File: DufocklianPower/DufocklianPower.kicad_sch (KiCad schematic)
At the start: 84 parts, among them J1 Conn_Receptacle_3P_Protected, J2 ST7796S, Q1 NMOS, Q2 NMOS, SW1 RST, SW2 BOOT, T1 Transformer_1P_1S, U2 LM5164DDA, U3 OPA388, U4 AD5282, U5 MCP4725, U6 ESP32-S3-WROOM-1, U7 INA228

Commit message: plotted again
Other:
- note added: "BUCK BOOST CONTROLLER"
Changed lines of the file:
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@@
+		)
+	)
+	(text "BUCK BOOST CONTROLLER"
+		(exclude_from_sim no)
+		(at 173.228 73.66 0)
+		(effects
+			(font
+				(size 1.27 1.27)
+			)
 		)
 	)

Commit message: finish pcb
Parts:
- removed C12: 1n, symbol Device:C
- removed C13, C29, C33, C34: 100n, symbol Device:C
- removed C14: 100u, symbol Device:C
- removed C28: 22n, symbol Device:C
- removed C30, C31, C32: 220u, symbol Device:C
- removed C35: 10u, symbol Device:C
- removed C4, C5: 10m, symbol Device:C
- removed D1: ABS2, Diode_SMD:Diode_Bridge_Diotec_ABS, symbol Diode_Bridge:ABS2
- removed D2: BAT54W, Package_TO_SOT_SMD:SOT-323_SC-70, symbol Diode:BAT54W
- removed J1: Conn_Receptacle_3P_Protected, symbol Connector:Conn_Receptacle_3P_Protected
- removed J2: ST7796S, symbol Connector_Generic:Conn_01x09
- removed L3: 1.5uH, symbol Device:L
- removed R15, R18: 11k, symbol Device:R
- removed R23: 6040, symbol Device:R
- removed T1: Transformer_1P_1S, symbol Device:Transformer_1P_1S
- removed U3: OPA388, Package_SO:SOIC-8_3.9x4.9mm_P1.27mm, symbol Amplifier_Operational:OPA333xxD
- removed U4: AD5282, Package_SO:TSSOP-16_4.4x5mm_P0.65mm, symbol Potentiometer_Digital:AD5282
- removed U5: MCP4725, Package_TO_SOT_SMD:SOT-23-6, symbol Analog_DAC:MCP4725xxx-xCH
- removed U7: INA228, Package_SO:TSSOP-10_3x3mm_P0.5mm, symbol Sensor_Energy:INA228
- added C4: 1u, Capacitor_SMD:C_0805_2012Metric, symbol Device:C_Small
- added C40: 100n, Capacitor_SMD:C_0805_2012Metric, symbol Device:C
- added C42: 100p, Capacitor_SMD:C_0805_2012Metric, symbol Device:C
- added C43: 1n, Capacitor_SMD:C_0805_2012Metric, symbol Device:C
- added C44: 2.2n, Capacitor_SMD:C_0805_2012Metric, symbol Device:C
- added J1, J3: 8174, Library:KEYSTONE_8174, symbol dufocklpwr:8174
- added J2: SCREEN, Connector_PinHeader_2.54mm:PinHeader_1x04_P2.54mm_Vertical, symbol Connector:Conn_01x04_Pin
- added J4: USB_C_Receptacle_USB2.0_14P, Connector_USB:USB_C_Receptacle_GCT_USB4105-xx-A_16P_TopMnt_Horizontal, symbol Connector:USB_C_Receptacle_USB2.0_14P
- added J5: OUT, Connector_AMASS:AMASS_XT60PW-M_1x02_P7.20mm_Horizontal, symbol Connector:Screw_Terminal_01x02
- added Q4: 2N7002, Package_TO_SOT_SMD:SOT-23, symbol Transistor_FET:2N7002
- added R23, R28: 2m, Library:FC4L90_OHM, symbol Device:R_Shunt
- added R29, R35: 2.7k, Resistor_SMD:R_0603_1608Metric, symbol Device:R
- added R30, R31: 5.1k, Resistor_SMD:R_0603_1608Metric, symbol Device:R
- added R32: 100k, Resistor_SMD:R_0603_1608Metric, symbol Device:R_45deg
- added R33, R34: 100, Resistor_SMD:R_0603_1608Metric, symbol Device:R_Small
- added SW3: Voltage Control, Rotary_Encoder:RotaryEncoder_Alps_EC11E-Switch_Vertical_H20mm, symbol Device:RotaryEncoder_Switch
- added SW4: Current Control, Rotary_Encoder:RotaryEncoder_Alps_EC11E-Switch_Vertical_H20mm, symbol Device:RotaryEncoder_Switch
- added U11: INA228, Package_SO:TSSOP-10_3x3mm_P0.5mm, symbol Sensor_Energy:INA228
- added U3: ADS8681RUM, Package_DFN_QFN:QFN-16-1EP_4x4mm_P0.65mm_EP2.7x2.7mm, symbol Analog_ADC:ADS8681RUM
- added U4: DAC8562, Package_SO:TSSOP-10_3x3mm_P0.5mm, symbol dufocklpwr:DAC8562
- added U5: INA241A4xD, Package_SO:SOIC-8_3.9x4.9mm_P1.27mm, symbol Amplifier_Current:INA241A4xD
- added U7: OPA188xxD, Package_SO:SOIC-8_3.9x4.9mm_P1.27mm, symbol Amplifier_Operational:OPA188xxD
- added U8: AP2112K-3.3, Package_TO_SOT_SMD:SOT-23-5, symbol Regulator_Linear:AP2112K-3.3
- added U9: REF6025xDGK, Package_SO:VSSOP-8_3x3mm_P0.65mm, symbol Reference_Voltage:REF6025xDGK
- C1, C19, C25, C36, C37, C38, C6, C7, C8: footprint (none) -> Capacitor_SMD:C_0805_2012Metric
- C10: value 470n -> 4.7u; footprint (none) -> Capacitor_SMD:C_0805_2012Metric
- C11: value 10n -> 10u; footprint (none) -> Capacitor_SMD:C_0805_2012Metric
- C15, C16, C17, C18, C21, C22, C23, C24: footprint (none) -> Capacitor_SMD:C_1210_3225Metric
- C2, C3: value 10m -> 1u; footprint (none) -> Capacitor_SMD:C_0805_2012Metric
- C20, C9: value 100n -> 1u; footprint (none) -> Capacitor_SMD:C_0805_2012Metric
- C26: value 2.2n -> 1u; footprint (none) -> Capacitor_SMD:C_0805_2012Metric
- C27: value 2.2n -> 47u; footprint (none) -> Capacitor_SMD:C_0805_2012Metric
- L1: footprint (none) -> Library:IND_SER2915H-223KL
- L2: footprint (none) -> Library:IND_BOURNS_SRR1260
- Q1, Q2: footprint (none) -> Library:TRANS_BSC027N10NS5ATMA1
- R1, R12, R13, R16, R17, R2, R24, R25, R26, R27, R3, R6: footprint (none) -> Resistor_SMD:R_0603_1608Metric
- R10: value 50k -> 14k7; footprint (none) -> Resistor_SMD:R_0603_1608Metric
- R11: value 470m -> 400k; footprint (none) -> Resistor_SMD:R_0603_1608Metric
- R14: value 1k -> 100k; footprint (none) -> Resistor_SMD:R_0603_1608Metric
- R19: value 10m -> 10k; footprint (none) -> Resistor_SMD:R_0603_1608Metric
- R20: value 121k -> 4.7k; footprint (none) -> Resistor_SMD:R_0603_1608Metric
- R21: value 1960 -> 120k; footprint (none) -> Resistor_SMD:R_0603_1608Metric
- R22: value 50 -> 5m; footprint (none) -> Resistor_SMD:R_0603_1608Metric
- R4: value 350k -> 316k; footprint (none) -> Resistor_SMD:R_0603_1608Metric
- R5: value 200k -> 101k; footprint (none) -> Resistor_SMD:R_0603_1608Metric
- R7: footprint (none) -> Resistor_SMD:R_2512_6332Metric
- R8: value 15 -> 615k; footprint (none) -> Resistor_SMD:R_0603_1608Metric
- R9: value 1k -> 10k; footprint (none) -> Resistor_SMD:R_0603_1608Metric
- SW1, SW2: footprint (none) -> Button_Switch_SMD:SW_Push_1P1T-SH_NO_CK_KMR2xxG
- U1: footprint (none) -> Library:VQFN24_RGY_TEX
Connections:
- net +3V3: now also C3.1, R26.1, C40.1, J2.2 (Pin_2), R29.1, R35.1, U11.6 (VS), U3.14 (DVDD), U4.9 (VDD), U8.5 (VOUT); no longer C6.2, L2.2, R26.2, R4.1
- net D+: now also J4.A6 (D+), J4.B6 (D+)
- net D-: now also J4.A7 (D-), J4.B7 (D-)
- net FB: now also R10.2, R8.2, R9.1; no longer R14.1
- net GND: now also C1.2, C10.1, C11.1, C15.2, C16.2, C17.2, C18.2, C19.2, C2.2, C20.2, C21.2, C22.2, C23.2, C24.2, C26.2, C27.2, C3.2, C36.2, C37.2, C38.2, C9.1, Q2.3 (S), R1.2, R13.2, R14.2, R21.2, R3.2, R5.2, R9.2, SW1.1, SW2.1, U1.1 (AVSS), U1.10 (PGND), U1.16 (VCCX), U1.18 (PFM/SYNC), U1.24 (REFAGND), U1.25 (GND), U1.7 (AGND), U2.1 (GND), U2.9 (EP), U6.1 (GND), U6.40 (GND), U6.41 (GND), C40.2, C44.1, J2.1 (Pin_1), J3.1, J3.2 (1__1), J3.3 (1__2), J3.4 (1__3), J4.A1 (GND), J4.A12 (GND), J4.B1 (GND), J4.B12 (GND), J4.SH (SHIELD), J5.1 (Pin_1), Q4.2 (S), R30.1, R31.2, R32.2, SW3.C, SW3.S2, SW4.C, SW4.S2, U11.1 (A1), U11.2 (A0), U11.7 (GND), U3.1 (AGND), U3.15 (DGND), U3.17 (PAD), U3.3 (REFGND), U3.6 (AIN_GND), U4.3 (GND), U5.2 (GND), U5.3 (REF2), U5.4 (GND), U5.7 (REF1), U7.4 (V-), U8.2 (GND), U9.7 (GND_F), U9.8 (GND_S); no longer R19.2
- net SCL: now also U6.11 (IO18), J2.3 (Pin_3), U11.5 (SCL); no longer U6.17 (IO9)
- net SDA: now also R26.2, U6.10 (IO17), J2.4 (Pin_4), U11.4 (SDA); no longer R26.1, U6.12 (IO8)
- net VBUS: now also C15.1, C16.1, C17.1, C18.1, Q1.1 (D), U1.12 (VIN), J1.1, J1.2 (1__1), J1.3 (1__2), J1.4 (1__3); no longer C10.1, C2.1, C3.1, C9.1, R11.1
- net VOUT_{0}: now also R11.2, R8.1, R23.1, R23.2, U5.8 (+); no longer R22.1
- net ~{ALRT}: now also U6.12 (IO8), U11.3 (~{Alert}); no longer U6.35 (IO42)
- net at R22.2: now also C27.1; no longer R20.1
- net at R20.2: now also Q4.3 (D); no longer R21.1
- net COMP: now reaches C36.1, R2.1, U1.5 (EXTCOMP)
- net COMP: now also R20.1
- net D_{IN}: now reaches U6.15 (IO3)
- net D_{IN}: now also U4.8 (D_{IN})
- net SCLK: now reaches U6.16 (IO46)
- net SCLK: now also U4.7 (SCLK)
- net ~{LDAC}: now reaches U6.18 (IO10)
- net ~{LDAC}: now also U4.4 (~{LDAC})
- net ~{CLR}: now reaches U6.19 (IO11)
- net ~{CLR}: now also U4.5 (~{CLR})
- net CEN_{A}: now reaches U6.23 (IO21)
- net CEN_{A}: now also SW4.A
- net VEN_{A}: now reaches U6.24 (IO47)
- net VEN_{A}: now also SW3.A
- net VEN_{B}: now reaches U6.25 (IO48)
- net VEN_{B}: now also SW3.B
- net V_{CF}: now reaches U6.26 (IO45)
- net V_{CF}: now also R29.2, SW3.S1
- net RVS: now reaches U6.31 (IO38)
- net RVS: now also U3.13 (RVS)
- net ALR: now reaches U6.32 (IO39)
- net ALR: now also U3.12 (SDO-1)
- net SDI: now reaches U6.38 (IO2)
- net SDI: now also U3.8 (SDI)
- net ~{RST}: now reaches U6.39 (IO1)
- net ~{RST}: now also U3.7 (~{RST})
- net BL renamed C_{CF}
- net C_{CF}: now also R35.2, SW4.S1
- net CS renamed CEN_{B}
- net CEN_{B}: now also SW4.B
- net DC: no longer names the net of U6.8 (IO15)
- removed net GNDREF: C1.2, C15.2, C16.2, C17.2, C18.2, C19.2, C2.2, C20.2, C21.2, C22.2, C23.2, C24.2, C3.2, C36.2, C37.2, C38.2, Q2.3 (S), R1.2, R13.2, R19.1, R21.2, R24.1, R3.2, R5.2, SW1.1, SW2.1, U1.1 (AVSS), U1.10 (PGND), U1.16 (VCCX), U1.18 (PFM/SYNC), U1.24 (REFAGND), U1.7 (AGND), U2.1 (GND), U2.9 (EP), U6.1 (GND), U6.40 (GND), U6.41 (GND)
- removed net INJ: C11.2, R10.2, R8.1, R9.1, U1.2 (INJ)
- removed net R1_{IN}: C26.2, C27.1, R16.2
- net R2_{IN}: no longer names the net of R24.2
- net R2_{IN}: now also Q4.1 (G), R32.1; no longer C27.2
- net RST: no longer names the net of U6.9 (IO16)
- net SDA_{0} renamed EN
- net EN: now also U1.19 (EN)
- removed net SENSE: C9.2, R10.1, U1.23 (SENSE)
- removed net VCC: C15.1, C16.1, C17.1, C18.1, Q1.1 (D), U1.12 (VIN), U1.19 (EN)
- net W_{1} renamed SDO
- net SDO: now also U3.11 (SDO-0)
- net W_{2} renamed CLK
- net CLK: now also U3.10 (SCLK)
- new net: C4.1, R34.1, U11.10 (Vin+)
- new net: C10.2, U3.2 (REFIO)
- new net: C4.2, R33.1, U11.9 (Vin-)
- new net: C42.1, C44.2, R16.2, R19.1, U7.3 (+)
- new net: C42.2, C43.2, R24.1, U7.6
- new net: J4.B5 (CC2), R30.2
- new net: R11.1, R14.1, U3.5 (AIN_P)
- new net: C43.1, R19.2
- new net: C11.2, C9.2, U3.4 (REFCAP)
- new net: C26.1, U9.4 (FILT)
- new net: J4.A5 (CC1), R31.1
- new net: R16.1, U5.5
- new net: R21.1, U9.3 (SS)
- new net +5V: C2.1, C6.2, J4.A4 (VBUS), J4.A9 (VBUS), J4.B4 (VBUS), J4.B9 (VBUS), L2.2, R4.1, U3.16 (AVDD), U5.6 (V+), U7.7 (V+), U8.1 (VIN), U8.3 (EN), U9.1 (VIN), U9.2 (EN)
- new net VOUT: J5.2 (Pin_2), R28.3, R28.4, R33.2
- new net VOUT_{1}: R23.3, R23.4, R28.1, R28.2, R34.2, U11.8 (Vbus), U5.1 (-)
- new net V_{REF}: R22.1, U4.10 (V_{REF}), U9.5 (OUT_S), U9.6 (OUT_F)
- new net ~{CC_{REF}}: U4.2 (V_{OUT}B), U7.2 (-)
- new net ~{CS}: U3.9 (CONVST/~{CS}), U6.35 (IO42)
- new net ~{SYNC}: U4.6 (~{SYNC}), U6.17 (IO9)
- new net ~{VC_{REF}}: R10.1, U4.1 (V_{OUT}A)
- no-connect marks 25 -> 14
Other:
- note added: "CC LOOP + COMP CLAMP"
- note added: "DIVIDER"
- note added: "Interface"
- note added: "POWER MOUNTS"
- note added: "REF DAC"
- note added: "REFERENCE VOLTAGE (2.5V)"
- note added: "SCREEN"
- note added: "USB PWR"
- note added: "USB RECEPTACLE"
- note added: "VOLTAGE LOOP ADC"
- note added: "Vout MONITOR"
- note removed: "**AS PER SNVAA85"
- note removed: "**CC LOOP"
- note removed: "**CV DIGIPOT"
- note removed: "**CV LOOP / DAC INJECTION **SEE SLVA861, SNVAA85(CV)"
- note removed: "**GNDin"
- note removed: "**GNDout"
- note removed: "**SEE SNVAA85"
- note removed: "3:1, V_{RMS}=~40V"
- note removed: "Active EMI Filter"
- note removed: "CURRENT SENSE RES"
- note removed: "DISPLAY"
- note removed: "MAINS POWER"
- note removed: "VOLTAGE/CURRENT SENSOR"
- note removed: "V_{BUS} = V_{RMS} * √2 V_{VBUS} = 40 * 1.414 V_{BUS} = 57V"
- moved on the sheet: C1, C15, C16, C17, C18, C19, C20, C21, C22, C23, C24, C25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

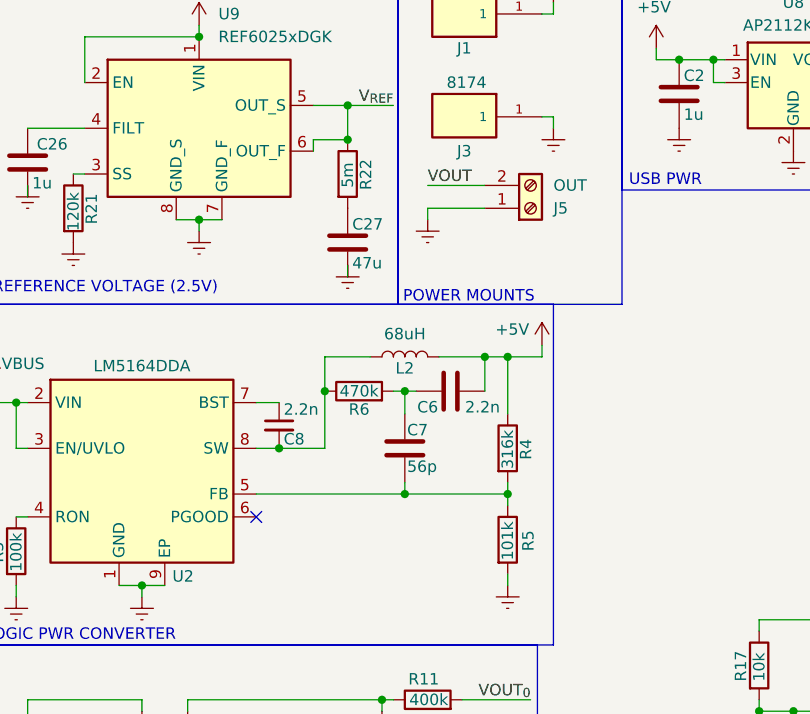
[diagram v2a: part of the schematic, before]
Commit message: finish via + change ind
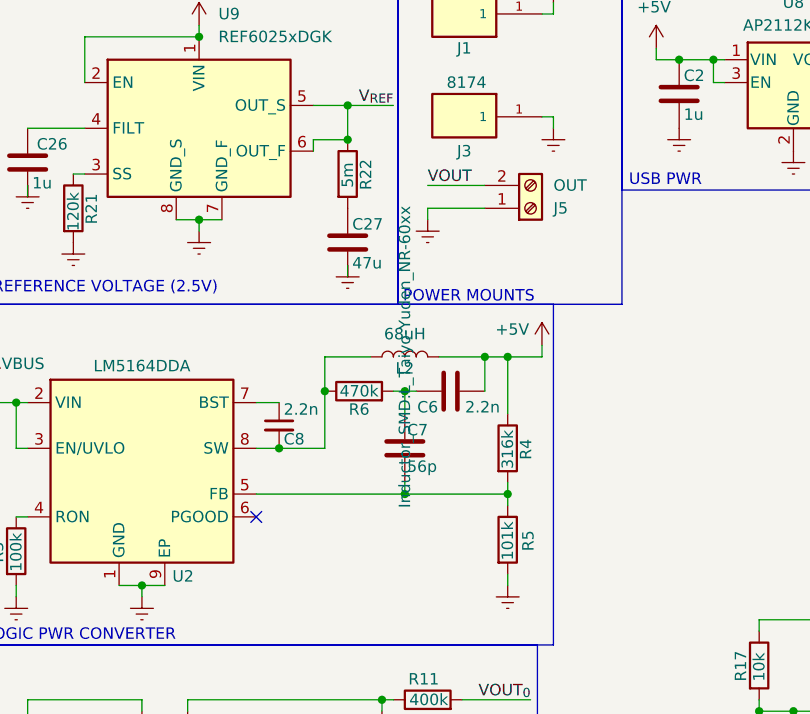
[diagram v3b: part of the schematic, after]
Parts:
- L2: footprint Library:IND_BOURNS_SRR1260 -> Inductor_SMD:L_Taiyo-Yuden_NR-60xx
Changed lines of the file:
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@@
 			)
 		)
-		(property "Footprint" "Library:IND_BOURNS_SRR1260"
+		(property "Footprint" "Inductor_SMD:L_Taiyo-Yuden_NR-60xx"
 			(at 59.69 55.88 0)
-			(hide yes)
 			(show_name no)
 			(do_not_autoplace no)

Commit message: bom.csv
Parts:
- removed J5: OUT, Connector_AMASS:AMASS_XT60PW-M_1x02_P7.20mm_Horizontal, symbol Connector:Screw_Terminal_01x02
- removed U7: OPA188xxD, Package_SO:SOIC-8_3.9x4.9mm_P1.27mm, symbol Amplifier_Operational:OPA188xxD
- added J6: Vout, Connector:Banana_Cliff_FCR7350Y_S16N-PC_Horizontal, symbol Connector:Screw_Terminal_01x01
- added J7: Screw_Terminal_01x01, Connector:Banana_Cliff_FCR7350Y_S16N-PC_Horizontal, symbol Connector:Screw_Terminal_01x01
- added U10: TLV3501AID, Package_SO:SOIC-8_3.9x4.9mm_P1.27mm, symbol Comparator:TLV3501AID
- C21: footprint Capacitor_SMD:C_1210_3225Metric -> Capacitor_SMD:C_Elec_10x10.2; now not fitted
- C22: footprint Capacitor_SMD:C_1210_3225Metric -> Capacitor_SMD:C_Elec_10x10.2
- C23, C24: footprint Capacitor_SMD:C_1210_3225Metric -> Capacitor_SMD:C_2220_5750Metric; now not fitted
- R11: footprint Resistor_SMD:R_0603_1608Metric -> Resistor_SMD:R_0805_2012Metric
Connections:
- net +5V: now also U10.7 (V+)
- net GND: now also J7.1 (Pin_1), U10.4 (V-), U10.8 (SHDN)
- net VOUT: now also J6.1 (Pin_1)
- net ~{CC_{REF}}: now also U10.2 (-)
- net at C42.1, C44.2, R16.2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: now also U10.3 (+)
- net at C42.2, C43.2, R24.1: now also U10.6
